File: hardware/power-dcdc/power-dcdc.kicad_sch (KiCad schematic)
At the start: 59 parts, among them J1 SOLAR_IN, J2 BATT2, J3 BATT1, Q1 SIR164ADP, Q2 SIR164ADP, Q3 SI7149ADP, Q4 SI7149ADP, Q5 SI7149ADP, Q6 SI7149ADP, U2 LP4951C, U3 NCP5901B, U4 PAC1953-1, U5 DGD0215, U6 DGD0215

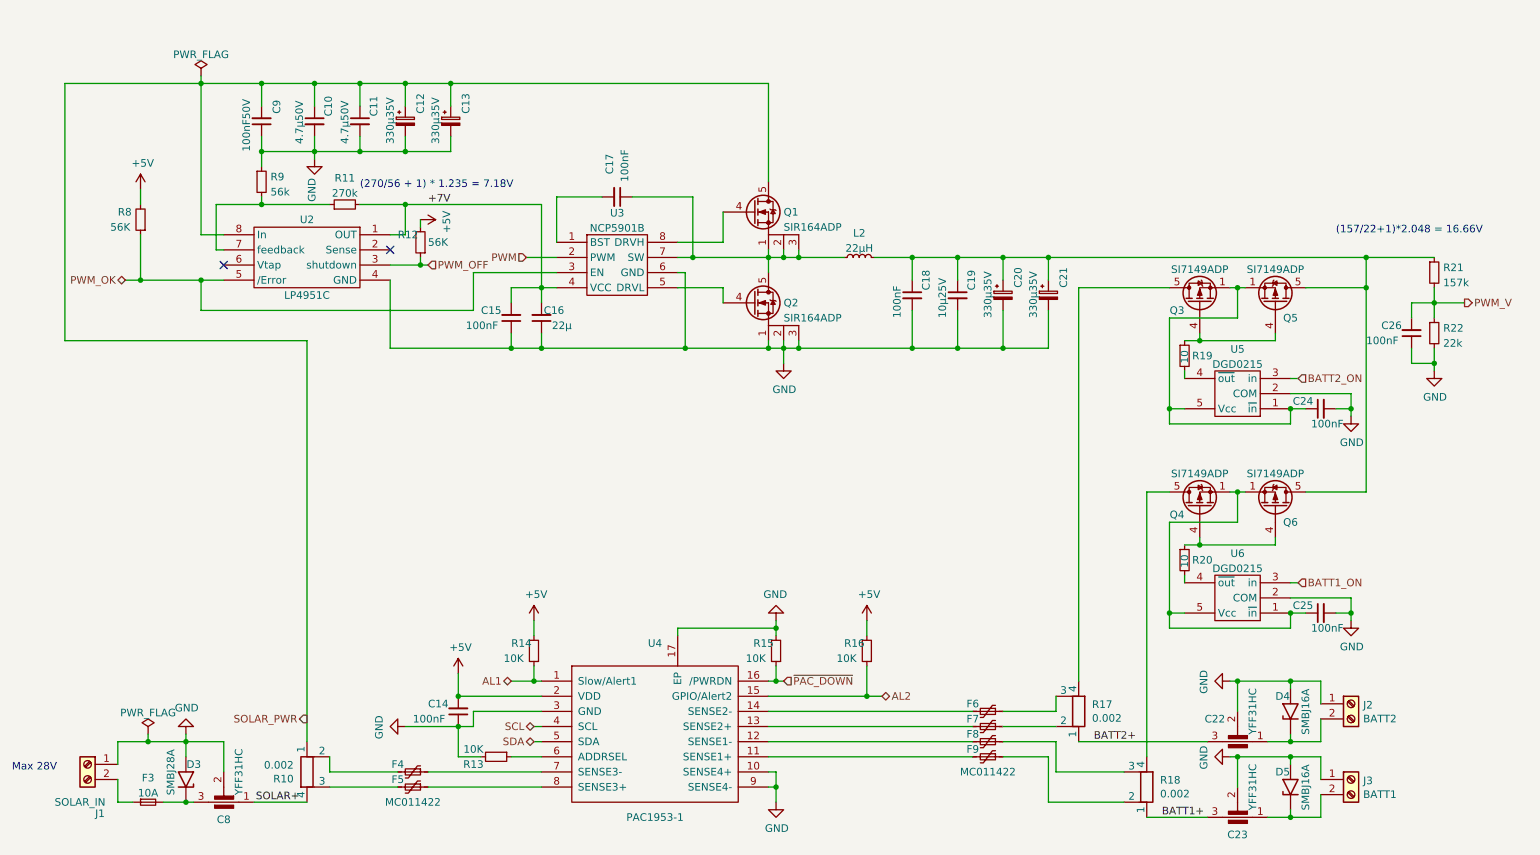
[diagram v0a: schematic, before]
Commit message: Split project in 2 boards: the power DC/DC and associated instrumentation, and control (with pic18 and canbus)
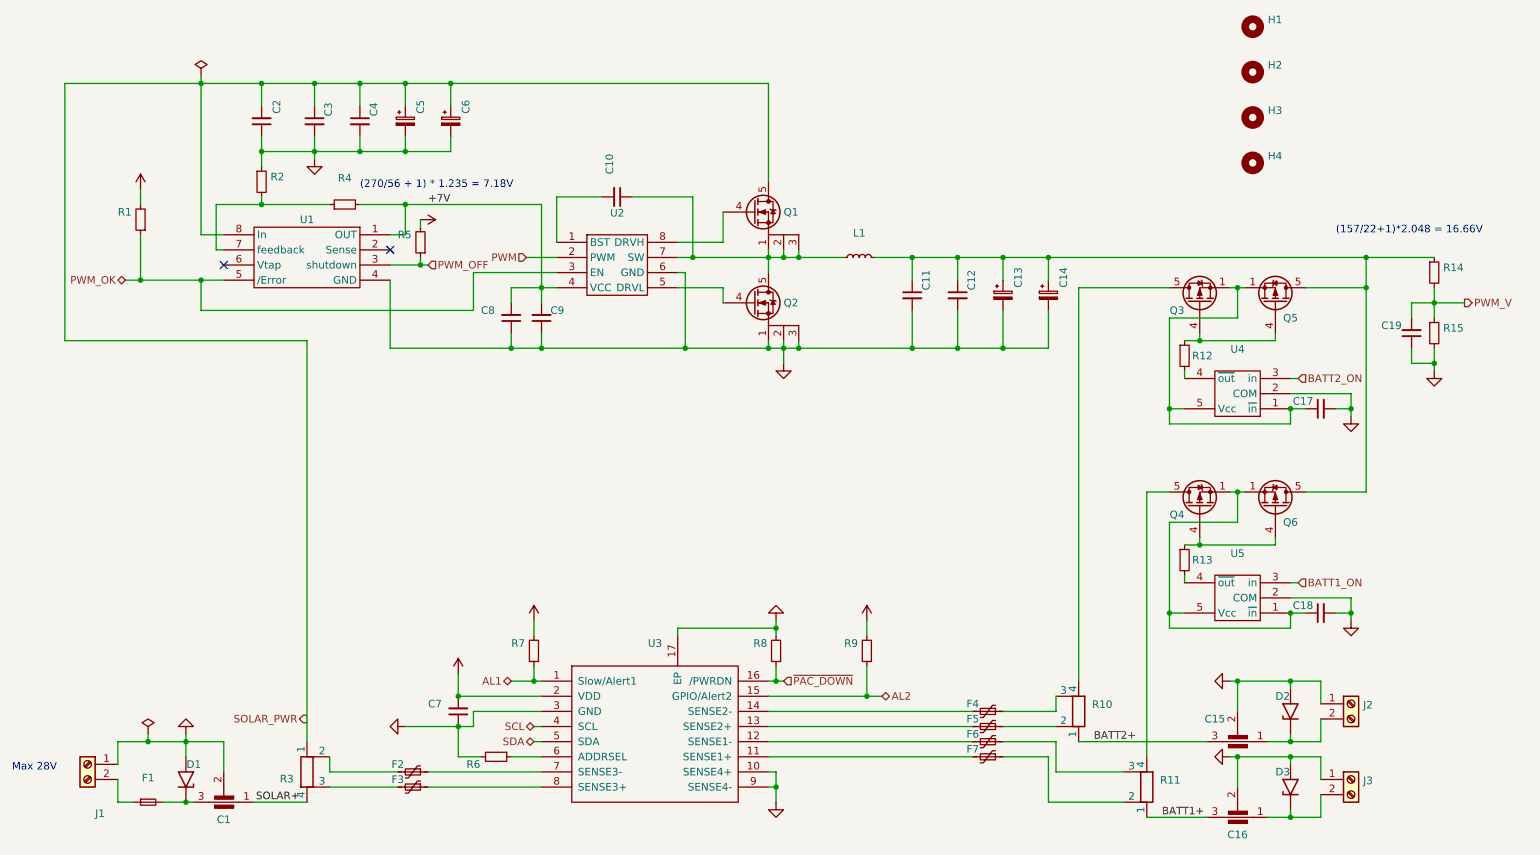
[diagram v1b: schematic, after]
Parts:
- added H1, H2, H3, H4: (no value), symbol Mechanical:MountingHole
- C1: renamed from C8; value YFF31HC -> (none); footprint local:C_filter_1206 -> (none)
- C10: renamed from C17; value 100nF -> (none); footprint Capacitor_SMD:C_0805_2012Metric_Pad1.18x1.45mm_HandSolder -> (none)
- C11: renamed from C18; value 100nF -> (none); footprint Capacitor_SMD:C_1206_3216Metric_Pad1.33x1.80mm_HandSolder -> (none)
- C12: renamed from C19; value 10µ25V -> (none); footprint Capacitor_SMD:C_1206_3216Metric_Pad1.33x1.80mm_HandSolder -> (none)
- C13: renamed from C20; value 330µ35V -> (none); footprint Capacitor_SMD:CP_Elec_10x12.6 -> (none)
- C14: renamed from C21; value 330µ35V -> (none); footprint Capacitor_SMD:CP_Elec_10x12.6 -> (none)
- C15: renamed from C22; value YFF31HC -> (none); footprint local:C_filter_1206 -> (none)
- C16: renamed from C23; value YFF31HC -> (none); footprint local:C_filter_1206 -> (none)
- C17: renamed from C24; value 100nF -> (none); footprint Capacitor_SMD:C_0603_1608Metric_Pad1.08x0.95mm_HandSolder -> (none)
- C18: renamed from C25; value 100nF -> (none); footprint Capacitor_SMD:C_0603_1608Metric_Pad1.08x0.95mm_HandSolder -> (none)
- C19: renamed from C26; value 100nF -> (none); footprint Capacitor_SMD:C_0805_2012Metric_Pad1.18x1.45mm_HandSolder -> (none)
- C2: renamed from C9; value 100nF50V -> (none); footprint Capacitor_SMD:C_0805_2012Metric_Pad1.18x1.45mm_HandSolder -> (none)
- C3: renamed from C10; value 4.7µ50V -> (none); footprint Capacitor_SMD:C_1206_3216Metric_Pad1.33x1.80mm_HandSolder -> (none)
- C4: renamed from C11; value 4.7µ50V -> (none); footprint Capacitor_SMD:C_1206_3216Metric_Pad1.33x1.80mm_HandSolder -> (none)
- C5: renamed from C12; value 330µ35V -> (none); footprint Capacitor_SMD:CP_Elec_10x12.6 -> (none)
- C6: renamed from C13; value 330µ35V -> (none); footprint Capacitor_SMD:CP_Elec_10x12.6 -> (none)
- C7: renamed from C14; value 100nF -> (none); footprint Capacitor_SMD:C_0805_2012Metric_Pad1.18x1.45mm_HandSolder -> (none)
- C8: renamed from C15; value 100nF -> (none); footprint Capacitor_SMD:C_0805_2012Metric_Pad1.18x1.45mm_HandSolder -> (none)
- C9: renamed from C16; value 22µ -> (none); footprint Capacitor_SMD:C_1206_3216Metric_Pad1.33x1.80mm_HandSolder -> (none)
- D1: renamed from D3; value SMBJ28A -> (none); footprint Diode_SMD:D_SMB_Handsoldering -> (none)
- D2: renamed from D4; value SMBJ16A -> (none); footprint Diode_SMD:D_SMB_Handsoldering -> (none)
- D3: renamed from D5; value SMBJ16A -> (none); footprint Diode_SMD:D_SMB_Handsoldering -> (none)
- F1: renamed from F3; value 10A -> (none); footprint Fuse:Fuseholder_Cylinder-5x20mm_Schurter_0031_8201_Horizontal_Open -> (none)
- F2: renamed from F4; value MC011422 -> (none); footprint Resistor_SMD:R_0603_1608Metric_Pad0.98x0.95mm_HandSolder -> (none)
- F3: renamed from F5; value MC011422 -> (none); footprint Resistor_SMD:R_0603_1608Metric_Pad0.98x0.95mm_HandSolder -> (none)
- F4: renamed from F6; value MC011422 -> (none); footprint Resistor_SMD:R_0603_1608Metric_Pad0.98x0.95mm_HandSolder -> (none)
- F5: renamed from F7; value MC011422 -> (none); footprint Resistor_SMD:R_0603_1608Metric_Pad0.98x0.95mm_HandSolder -> (none)
- F6: renamed from F8; value MC011422 -> (none); footprint Resistor_SMD:R_0603_1608Metric_Pad0.98x0.95mm_HandSolder -> (none)
- F7: renamed from F9; value MC011422 -> (none); footprint Resistor_SMD:R_0603_1608Metric_Pad0.98x0.95mm_HandSolder -> (none)
- J1: value SOLAR_IN -> (none); footprint TerminalBlock_MetzConnect:TerminalBlock_MetzConnect_Type703_RT10N02HGLU_1x02_P9.52mm_Horizontal -> (none)
- J2: value BATT2 -> (none); footprint TerminalBlock_MetzConnect:TerminalBlock_MetzConnect_Type703_RT10N02HGLU_1x02_P9.52mm_Horizontal -> (none)
- J3: value BATT1 -> (none); footprint TerminalBlock_MetzConnect:TerminalBlock_MetzConnect_Type703_RT10N02HGLU_1x02_P9.52mm_Horizontal -> (none)
- L1: renamed from L2; value 22µH -> (none); footprint Inductor_THT:L_Toroid_Horizontal_D32.5mm_P30.00mm_Bourns_2300 -> (none)
- Q1, Q2: value SIR164ADP -> (none); footprint Package_SO:PowerPAK_SO-8_Single -> (none)
- Q3, Q4, Q5, Q6: value SI7149ADP -> (none); footprint Package_SO:PowerPAK_SO-8_Single -> (none)
- R1: renamed from R8; value 56K -> (none); footprint Resistor_SMD:R_1206_3216Metric_Pad1.30x1.75mm_HandSolder -> (none)
- R10: renamed from R17; value 0.002 -> (none); footprint local:R-Shunt_2512_6332Metric_Pad1.40x3.35mm_HandSolder -> (none)
- R11: renamed from R18; value 0.002 -> (none); footprint local:R-Shunt_2512_6332Metric_Pad1.40x3.35mm_HandSolder -> (none)
- R12: renamed from R19; value 10 -> (none); footprint Resistor_SMD:R_0805_2012Metric_Pad1.20x1.40mm_HandSolder -> (none)
- R13: renamed from R20; value 10 -> (none); footprint Resistor_SMD:R_0805_2012Metric_Pad1.20x1.40mm_HandSolder -> (none)
- R14: renamed from R21; value 157k -> (none); footprint Resistor_SMD:R_0805_2012Metric_Pad1.20x1.40mm_HandSolder -> (none)
- R15: renamed from R22; value 22k -> (none); footprint Resistor_SMD:R_0805_2012Metric_Pad1.20x1.40mm_HandSolder -> (none)
- R2: renamed from R9; value 56k -> (none); footprint Resistor_SMD:R_1206_3216Metric_Pad1.30x1.75mm_HandSolder -> (none)
- R3: renamed from R10; value 0.002 -> (none); footprint local:R-Shunt_2512_6332Metric_Pad1.40x3.35mm_HandSolder -> (none)
- R4: renamed from R11; value 270k -> (none); footprint Resistor_SMD:R_0805_2012Metric_Pad1.20x1.40mm_HandSolder -> (none)
- R5: renamed from R12; value 56K -> (none); footprint Resistor_SMD:R_1206_3216Metric_Pad1.30x1.75mm_HandSolder -> (none)
- R6: renamed from R13; value 10K -> (none); footprint Resistor_SMD:R_0805_2012Metric_Pad1.20x1.40mm_HandSolder -> (none)
- R7: renamed from R14; value 10K -> (none); footprint Resistor_SMD:R_0805_2012Metric_Pad1.20x1.40mm_HandSolder -> (none)
- R8: renamed from R15; value 10K -> (none); footprint Resistor_SMD:R_0805_2012Metric_Pad1.20x1.40mm_HandSolder -> (none)
- R9: renamed from R16; value 10K -> (none); footprint Resistor_SMD:R_0805_2012Metric_Pad1.20x1.40mm_HandSolder -> (none)
- U1: renamed from U2; value LP4951C -> (none); footprint Package_SO:SOIC-8_3.9x4.9mm_P1.27mm -> (none)
- U2: renamed from U3; value NCP5901B -> (none); footprint Package_SO:SOIC-8_3.9x4.9mm_P1.27mm -> (none)
- U3: renamed from U4; value PAC1953-1 -> (none); footprint local:VQFN-16-1EP_3x3mm_P0.5mm_EP1.1x1.1mm -> (none)
- U4: renamed from U5; value DGD0215 -> (none); footprint Package_TO_SOT_SMD:TSOT-23-5 -> (none)
- U5: renamed from U6; value DGD0215 -> (none); footprint Package_TO_SOT_SMD:TSOT-23-5 -> (none)

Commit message: Add board-to-board connectors.
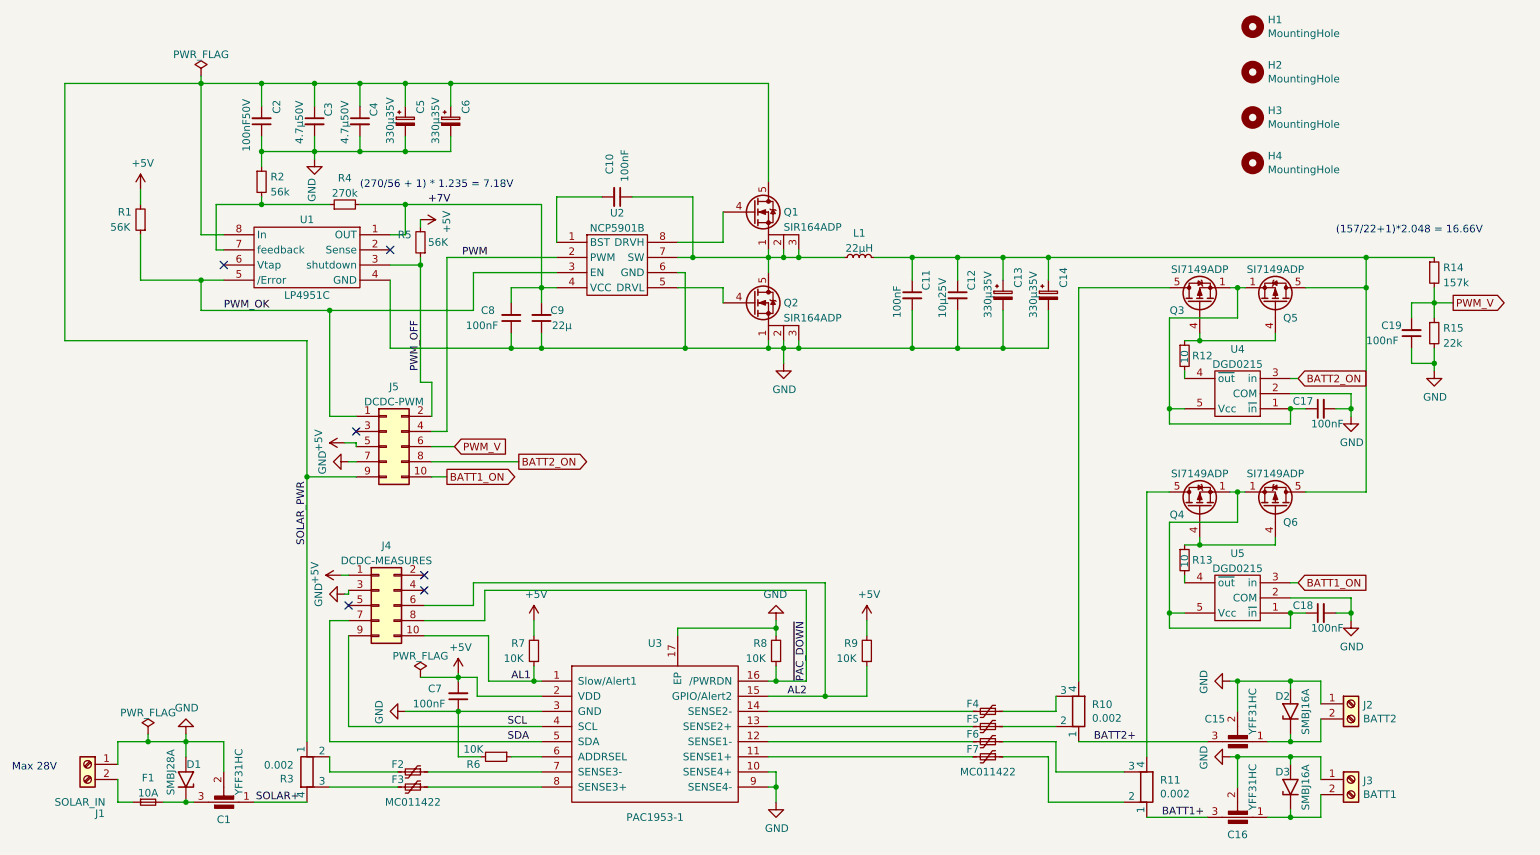
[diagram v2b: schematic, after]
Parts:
- added J4: DCDC-MEASURES, symbol Connector_Generic:Conn_02x05_Odd_Even
- added J5: DCDC-PWM, symbol Connector_Generic:Conn_02x05_Odd_Even
- C1, C15, C16: value (none) -> YFF31HC; footprint (none) -> local:C_filter_1206
- C10, C19, C7, C8: value (none) -> 100nF; footprint (none) -> Capacitor_SMD:C_0805_2012Metric_Pad1.18x1.45mm_HandSolder
- C11: value (none) -> 100nF; footprint (none) -> Capacitor_SMD:C_1206_3216Metric_Pad1.33x1.80mm_HandSolder
- C12: value (none) -> 10µ25V; footprint (none) -> Capacitor_SMD:C_1206_3216Metric_Pad1.33x1.80mm_HandSolder
- C13, C14, C5, C6: value (none) -> 330µ35V; footprint (none) -> Capacitor_SMD:CP_Elec_10x12.6
- C17, C18: value (none) -> 100nF; footprint (none) -> Capacitor_SMD:C_0603_1608Metric_Pad1.08x0.95mm_HandSolder
- C2: value (none) -> 100nF50V; footprint (none) -> Capacitor_SMD:C_0805_2012Metric_Pad1.18x1.45mm_HandSolder
- C3, C4: value (none) -> 4.7µ50V; footprint (none) -> Capacitor_SMD:C_1206_3216Metric_Pad1.33x1.80mm_HandSolder
- C9: value (none) -> 22µ; footprint (none) -> Capacitor_SMD:C_1206_3216Metric_Pad1.33x1.80mm_HandSolder
- D1: value (none) -> SMBJ28A; footprint (none) -> Diode_SMD:D_SMB_Handsoldering
- D2, D3: value (none) -> SMBJ16A; footprint (none) -> Diode_SMD:D_SMB_Handsoldering
- F1: value (none) -> 10A; footprint (none) -> Fuse:Fuseholder_Cylinder-5x20mm_Schurter_0031_8201_Horizontal_Open
- F2, F3, F4, F5, F6, F7: value (none) -> MC011422; footprint (none) -> Resistor_SMD:R_0603_1608Metric_Pad0.98x0.95mm_HandSolder
- H1, H2, H3, H4: value (none) -> MountingHole; footprint (none) -> MountingHole:MountingHole_3.2mm_M3_DIN965
- J1: value (none) -> SOLAR_IN; footprint (none) -> TerminalBlock_MetzConnect:TerminalBlock_MetzConnect_Type703_RT10N02HGLU_1x02_P9.52mm_Horizontal
- J2: value (none) -> BATT2; footprint (none) -> TerminalBlock_MetzConnect:TerminalBlock_MetzConnect_Type703_RT10N02HGLU_1x02_P9.52mm_Horizontal
- J3: value (none) -> BATT1; footprint (none) -> TerminalBlock_MetzConnect:TerminalBlock_MetzConnect_Type703_RT10N02HGLU_1x02_P9.52mm_Horizontal
- L1: value (none) -> 22µH; footprint (none) -> Inductor_THT:L_Toroid_Horizontal_D32.5mm_P30.00mm_Bourns_2300
- Q1, Q2: value (none) -> SIR164ADP; footprint (none) -> Package_SO:PowerPAK_SO-8_Single
- Q3, Q4, Q5, Q6: value (none) -> SI7149ADP; footprint (none) -> Package_SO:PowerPAK_SO-8_Single
- R1, R5: value (none) -> 56K; footprint (none) -> Resistor_SMD:R_1206_3216Metric_Pad1.30x1.75mm_HandSolder
- R10, R11, R3: value (none) -> 0.002; footprint (none) -> local:R-Shunt_2512_6332Metric_Pad1.40x3.35mm_HandSolder
- R12, R13: value (none) -> 10; footprint (none) -> Resistor_SMD:R_0805_2012Metric_Pad1.20x1.40mm_HandSolder
- R14: value (none) -> 157k; footprint (none) -> Resistor_SMD:R_0805_2012Metric_Pad1.20x1.40mm_HandSolder
- R15: value (none) -> 22k; footprint (none) -> Resistor_SMD:R_0805_2012Metric_Pad1.20x1.40mm_HandSolder
- R2: value (none) -> 56k; footprint (none) -> Resistor_SMD:R_1206_3216Metric_Pad1.30x1.75mm_HandSolder
- R4: value (none) -> 270k; footprint (none) -> Resistor_SMD:R_0805_2012Metric_Pad1.20x1.40mm_HandSolder
- R6, R7, R8, R9: value (none) -> 10K; footprint (none) -> Resistor_SMD:R_0805_2012Metric_Pad1.20x1.40mm_HandSolder
- U1: value (none) -> LP4951C; footprint (none) -> Package_SO:SOIC-8_3.9x4.9mm_P1.27mm
- U2: value (none) -> NCP5901B; footprint (none) -> Package_SO:SOIC-8_3.9x4.9mm_P1.27mm
- U3: value (none) -> PAC1953-1; footprint (none) -> local:VQFN-16-1EP_3x3mm_P0.5mm_EP1.1x1.1mm
- U4, U5: value (none) -> DGD0215; footprint (none) -> Package_TO_SOT_SMD:TSOT-23-5
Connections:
- net +5V: now also J4.1 (Pin_1), J5.5 (Pin_5)
- net AL1: now also J4.10 (Pin_10)
- net AL2: now also J4.6 (Pin_6)
- net BATT1_ON: now also J5.10 (Pin_10)
- net BATT2_ON: now also J5.8 (Pin_8)
- net GND: now also J4.3 (Pin_3), J5.7 (Pin_7)
- net PWM: now also J5.4 (Pin_4)
- net PWM_OFF: now also J5.2 (Pin_2)
- net PWM_OK: now also J5.1 (Pin_1)
- net PWM_V: now also J5.6 (Pin_6)
- net SCL: now also J4.9 (Pin_9)
- net SDA: now also J4.7 (Pin_7)
- net SOLAR_PWR: now also J5.9 (Pin_9)
- net ~{PAC_DOWN}: now also J4.8 (Pin_8)
- no-connect marks 2 -> 6
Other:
- moved on the sheet: C7
